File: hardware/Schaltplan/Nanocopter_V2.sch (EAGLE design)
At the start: 89 parts, among them M1+ TPTP15SQ, M1- TPTP15SQ, M2+ TPTP15SQ, M2- TPTP15SQ, M3+ TPTP15SQ, M3- TPTP15SQ, M4+ TPTP15SQ, M4- TPTP15SQ, T1 IRLML2502, T2 IRLML2502, T3 IRLML2502, T4 IRLML2502, U2 PRTR5V0U2X, U3 LM3480-3.3, X1 USBSMD

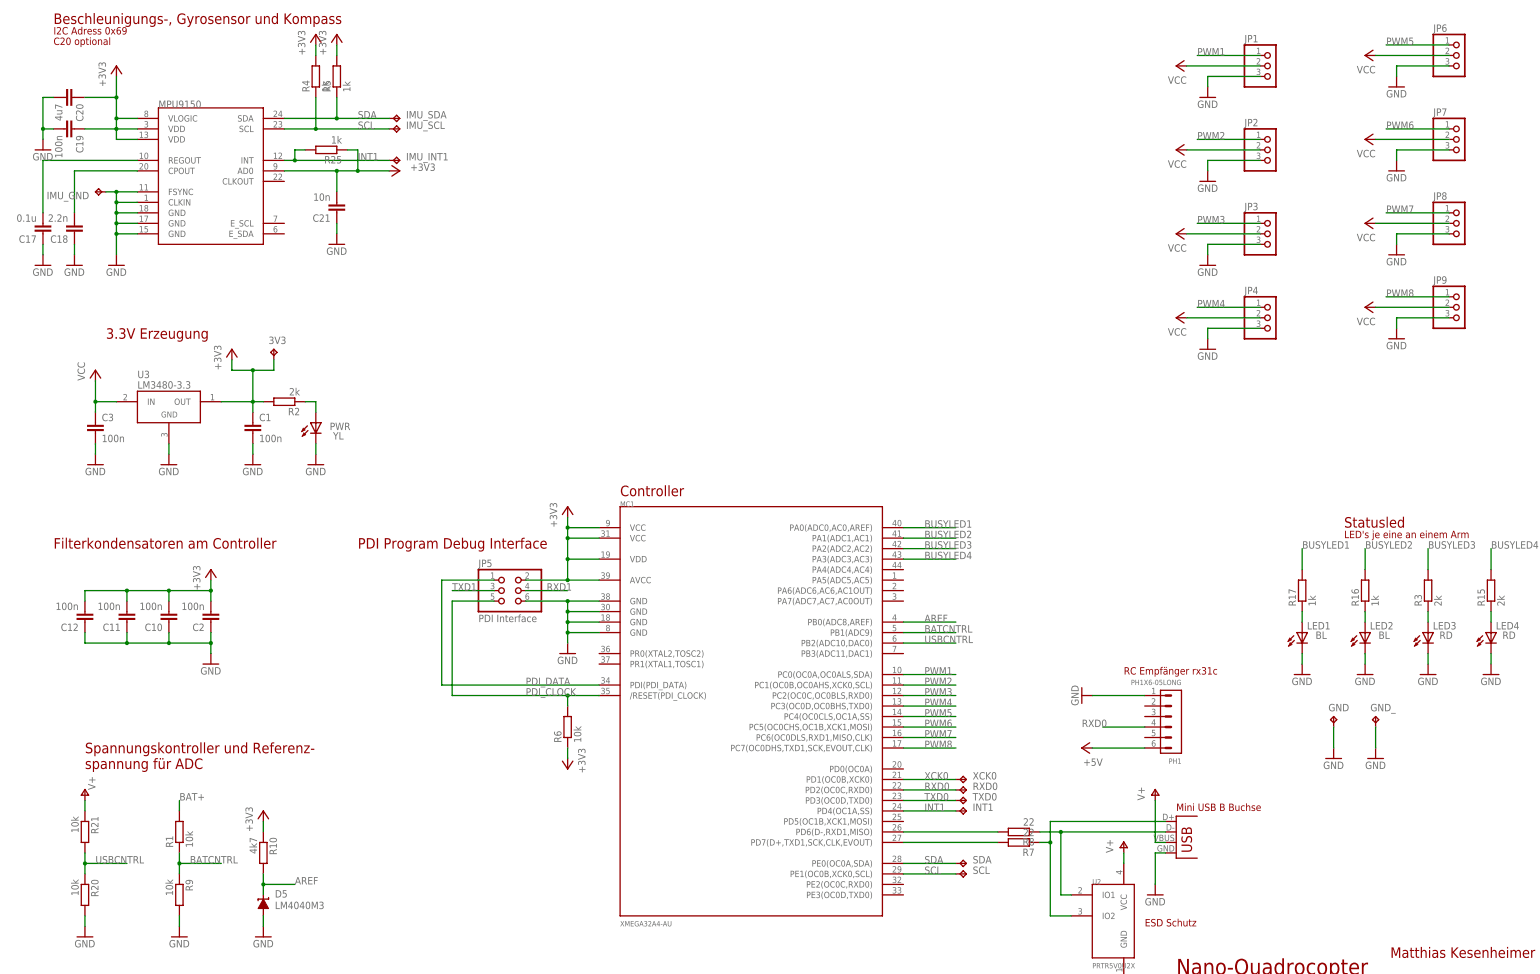
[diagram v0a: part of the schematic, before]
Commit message: Neuer Schaltplan V2.1. Die Schaltung wird jetzt in zwei Teile aufgeteilt: Flugcontroller (SimpleControl) und Motortreiber-platine (BaseFrame).
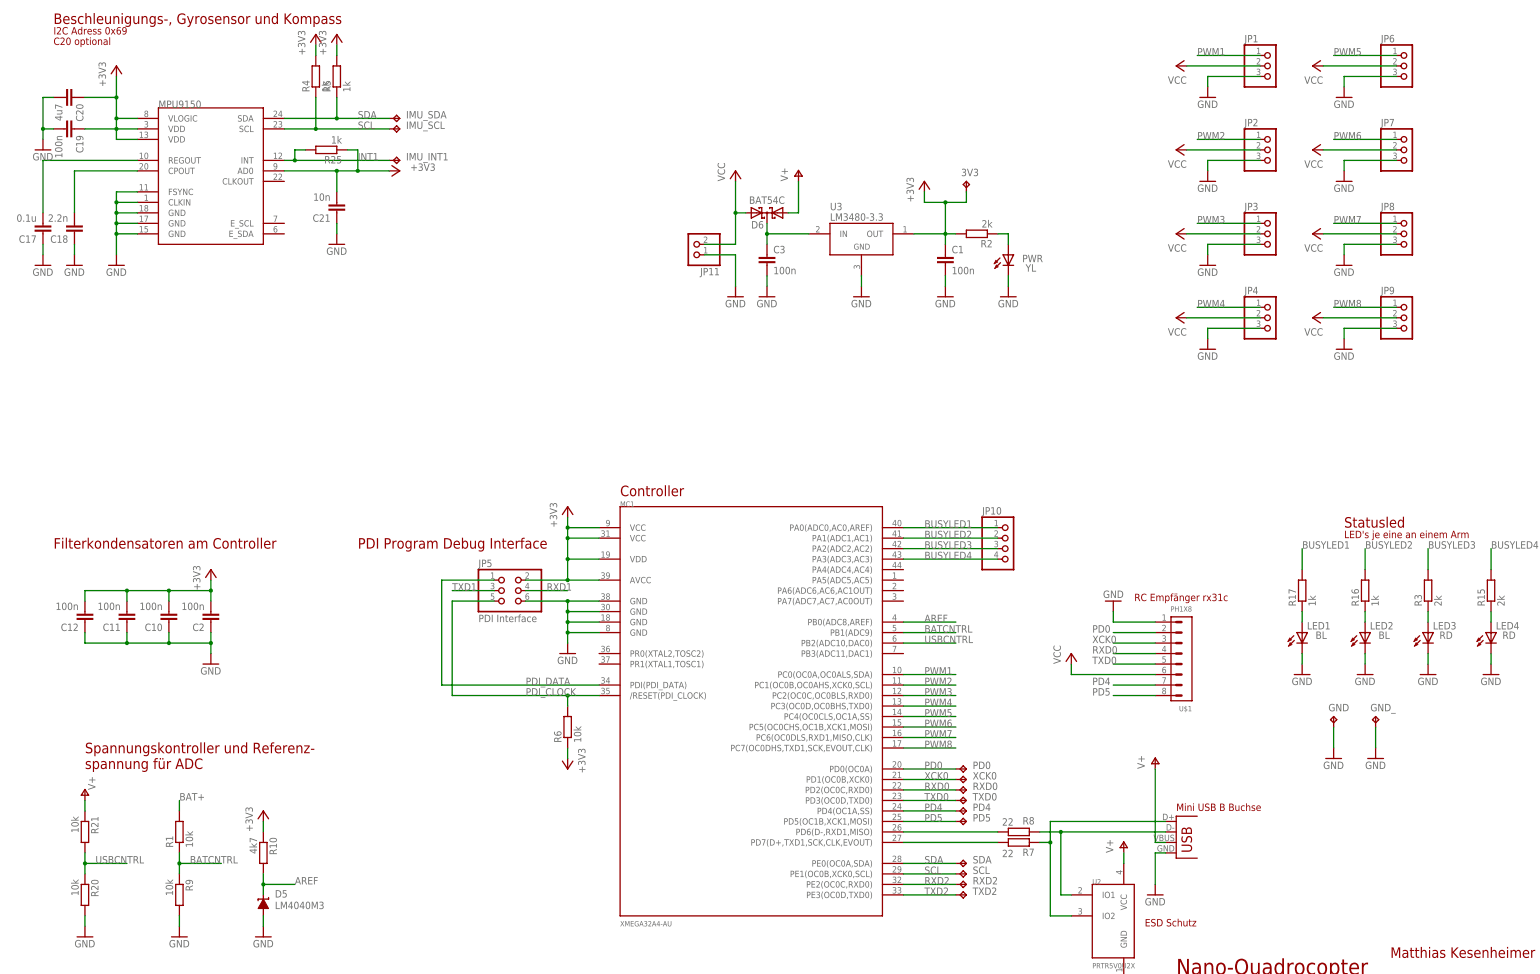
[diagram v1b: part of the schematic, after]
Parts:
- removed IMU_GND: TPTP10SQ, testpad:TPTP10SQ
- removed PH1: PH1X6-05LONG, pel_hdr:PH1X6-05LONG
- added D6: BAT54C, diode:BAT54C
- added JP10: (no value), pinhead:PINHD-1X4
- added JP11: (no value), pinhead:PINHD-1X2
- added PD0, PD5, RXD2, TXD2: TPTP10SQ, testpad:TPTP10SQ
- added U$1: PH1X8, pel_hdr:PH1X8
- renumbered INT1 to PD4
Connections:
- removed net +5V: PH1.6
- new net N$6: C3.1, D6.CC, U3.IN
- new net PD0: MC1.PD0(OC0A), PD0.TP, U$1.2
- new net PD4: MC1.PD4(OC1A,SS), PD4.TP, U$1.7
- new net PD5: MC1.PD5(OC1B,XCK1,MOSI), PD5.TP, U$1.8
- new net RXD2: MC1.PE2(OC0C,RXD0), RXD2.TP
- new net TXD2: MC1.PE3(OC0D,TXD0), TXD2.TP
- net BUSYLED1: now also JP10.1
- net BUSYLED2: now also JP10.2
- net BUSYLED3: now also JP10.3
- net BUSYLED4: now also JP10.4
- net GND: now also JP11.1, U$1.1; no longer IMU_GND.TP, PH1.1
- net INT1: no longer MC1.PD4(OC1A,SS), PD4.TP
- net RXD0: now also U$1.4; no longer PH1.4
- net TXD0: now also U$1.5
- net V+: now also D6.A1
- net VCC: now also D6.A2, JP11.2, U$1.6; no longer C3.1, U3.IN
- net XCK0: now also U$1.3
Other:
- note removed: "3.3V Erzeugung"
- moved on the sheet: 3V3, C1, C3, JP6, JP7, JP8, JP9, PWR, R2, U3
